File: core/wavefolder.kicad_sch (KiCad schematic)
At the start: 43 parts, among them U10 TL072

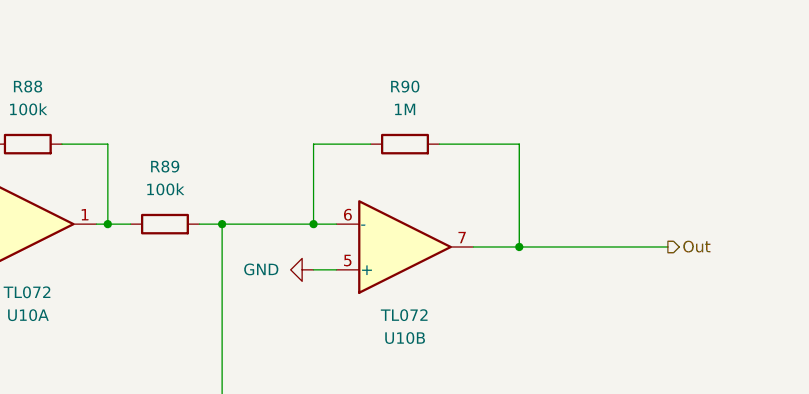
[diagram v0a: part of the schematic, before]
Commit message: Tweak resistor values
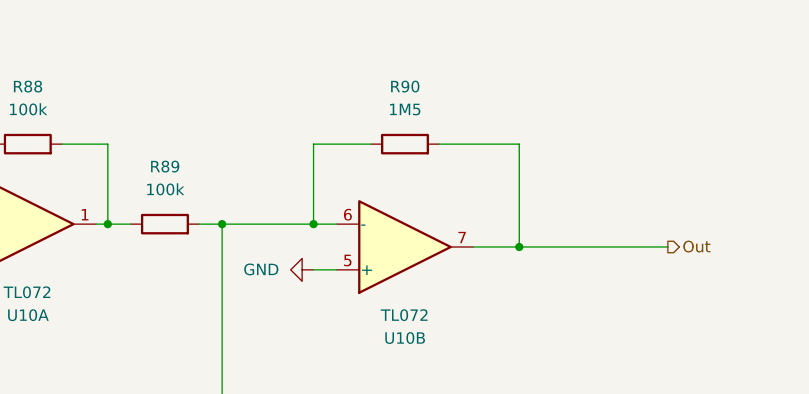
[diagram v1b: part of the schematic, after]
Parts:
- R90: value 1M -> 1M5
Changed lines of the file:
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@@
 			)
 		)
-		(property "Value" "1M"
+		(property "Value" "1M5"
 			(at 177.8 54.61 90)
 			(effects

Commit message: Update partnames
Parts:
- D39, D40, D41, D42, D43, D44, D45, D46, D47, D48, D49, D50, D51, D52, D53, D54, D55, D56, D57, D58, D59, D60, D61, D62: value D -> 1N4148
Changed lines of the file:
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@@
 			)
 		)
-		(property "Value" "D"
+		(property "Value" "1N4148"
 			(at 92.71 58.4199 90)
 			(effects
@@
 			)
 		)
-		(property "Value" "D"
+		(property "Value" "1N4148"
 			(at 60.96 90.1699 90)
 			(effects
@@
 			)
 		)
-		(property "Value" "D"
+		(property "Value" "1N4148"
 			(at 46.99 110.4899 90)
 			(effects
@@
 			)
 		)
-		(property "Value" "D"
+		(property "Value" "1N4148"
 			(at 60.96 69.8499 90)
 			(effects
@@
 			)
 		)
-		(property "Value" "D"
+		(property "Value" "1N4148"
 			(at 96.52 80.0099 90)
 			(effects
@@
 			)
 		)
-		(property "Value" "D"
+		(property "Value" "1N4148"
 			(at 46.99 69.8499 90)
 			(effects
@@
 			)
 		)
-		(property "Value" "D"
+		(property "Value" "1N4148"
 			(at 69.85 100.3299 90)
 			(effects
@@
 			)
 		)
-		(property "Value" "D"
+		(property "Value" "1N4148"
 			(at 46.99 90.1699 90)
 			(effects
@@
 			)
 		)
-		(property "Value" "D"
+		(property "Value" "1N4148"
 			(at 69.85 69.8499 90)
 			(effects
@@
 			)
 		)
-		(property "Value" "D"
+		(property "Value" "1N4148"
 			(at 38.1 69.8499 90)
 			(effects
@@
 			)
 		)
-		(property "Value" "D"
+		(property "Value" "1N4148"
 			(at 60.96 80.0099 90)
 			(effects
@@
 			)
 		)
-		(property "Value" "D"
+		(property "Value" "1N4148"
 			(at 87.63 100.3299 90)
 			(effects
@@
 			)
 		)
-		(property "Value" "D"
+		(property "Value" "1N4148"
 			(at 87.63 80.0099 90)
 			(effects
@@
 			)
 		)
-		(property "Value" "D"
+		(property "Value" "1N4148"
 			(at 96.52 100.3299 90)
 			(effects
@@
 			)
 		)
-		(property "Value" "D"
+		(property "Value" "1N4148"
 			(at 60.96 59.6899 90)
 			(effects
@@
 			)
 		)
-		(property "Value" "D"
+		(property "Value" "1N4148"
 			(at 60.96 100.3299 90)
 			(effects
@@
 			)
 		)
-		(property "Value" "D"
+		(property "Value" "1N4148"
 			(at 83.82 58.4199 90)
 			(effects
@@
 			)
 		)
-		(property "Value" "D"
+		(property "Value" "1N4148"
 			(at 69.85 80.0099 90)
 			(effects
@@
 			)
 		)
-		(property "Value" "D"
+		(property "Value" "1N4148"
 			(at 38.1 90.1699 90)
 			(effects
@@
 			)
 		)
-		(property "Value" "D"
+		(property "Value" "1N4148"
 			(at 38.1 110.4899 90)
 			(effects
@@
 			)
 		)
-		(property "Value" "D"
+		(property "Value" "1N4148"
 			(at 69.85 59.6899 90)
 			(effects
@@
 			)
 		)
-		(property "Value" "D"
+		(property "Value" "1N4148"
 			(at 69.85 110.4899 90)
 			(effects
@@
 			)
 		)
-		(property "Value" "D"
+		(property "Value" "1N4148"
 			(at 60.96 110.4899 90)
 			(effects
@@
 			)
 		)
-		(property "Value" "D"
+		(property "Value" "1N4148"
 			(at 69.85 90.1699 90)
 			(effects

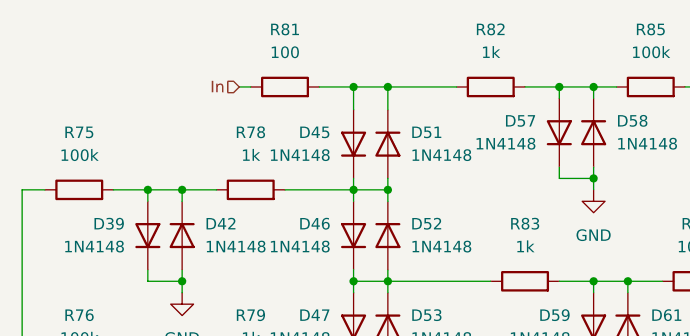
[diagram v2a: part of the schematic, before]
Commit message: Change to safer resistor value
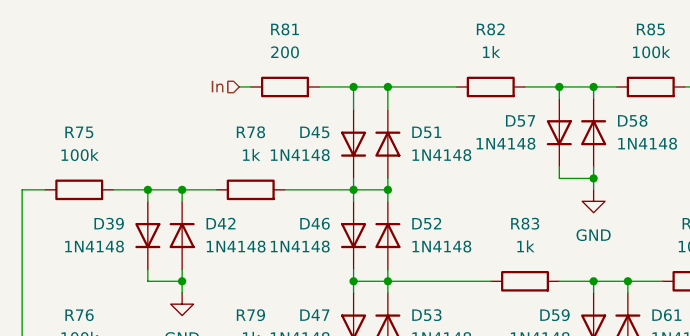
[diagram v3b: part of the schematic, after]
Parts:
- R81: value 100 -> 200
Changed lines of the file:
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@@
 			)
 		)
-		(property "Value" "100"
+		(property "Value" "200"
 			(at 55.88 48.26 90)
 			(effects

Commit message: Fixes for v1.1
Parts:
- added C15: 470n C0G, Capacitor_SMD:C_1206_3216Metric, symbol Device:C
- renumbered C19 to C13, C20 to C14, D42 to D10, D43 to D11, D44 to D12, D45 to D13, D46 to D14, D47 to D15, D48 to D16, D49 to D17, D50 to D18, D51 to D19, D52 to D20, D53 to D21, D54 to D22, D55 to D23, D56 to D24, D57 to D25, D58 to D26, D59 to D27, D60 to D28, D61 to D29, D62 to D30, D39 to D7, D40 to D8, D41 to D9, R75 to R39, R76 to R40, R77 to R41, R78 to R42, R79 to R43, R80 to R44, R81 to R45, R82 to R46, R83 to R47, R84 to R48, R85 to R49, R86 to R50, R87 to R51, R88 to R52, R89 to R53, R90 to R54, U10 to U7
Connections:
- net Out: now also C15.2; no longer R54.2, U7.7
- new net: C15.1, R54.2, U7.7
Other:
- moved on the sheet: C13, C14, D13, D14, D15, D16, D17, D18, D19, D20, D21, D22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
